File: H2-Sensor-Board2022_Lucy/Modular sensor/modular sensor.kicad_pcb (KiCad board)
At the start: 2 copper layers, 55.1 x 30.5 mm, 8 parts, among them J1 Conn_01x03_Pin

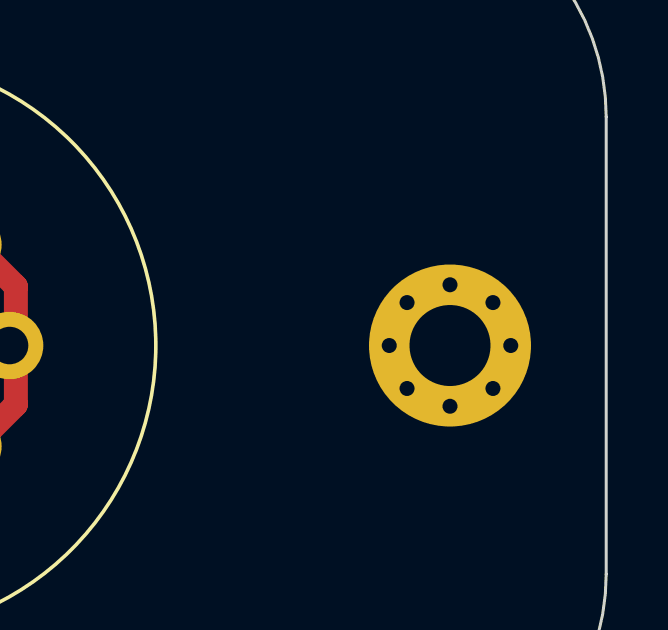
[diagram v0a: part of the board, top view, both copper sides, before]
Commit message: Started Layout fixed footprint for daughter baord and added M3 mounting holes.
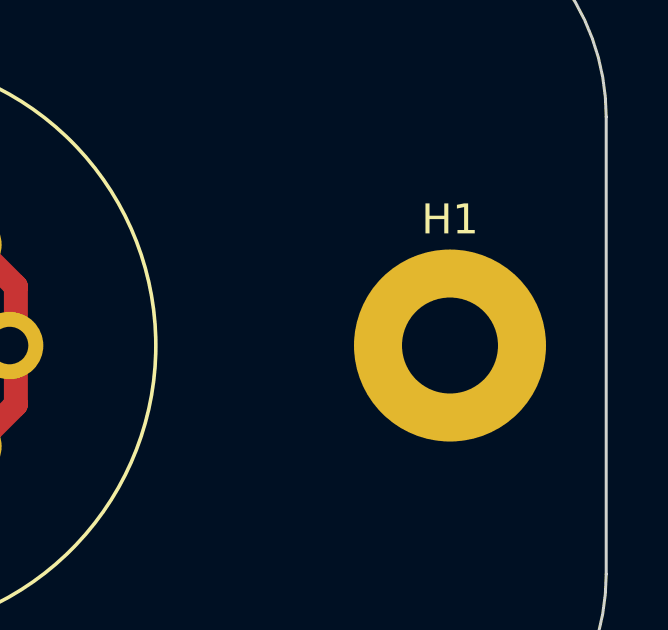
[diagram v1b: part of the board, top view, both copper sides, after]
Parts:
- H1: footprint MountingHole:MountingHole_2.7mm_M2.5_Pad_Via -> MountingHole:MountingHole_3.2mm_M3_Pad
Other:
- board text added: "Simon W."
- board text removed: "sw"
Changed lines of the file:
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@@
     )
   )
-  (footprint "MountingHole:MountingHole_2.7mm_M2.5_Pad_Via" (layer "F.Cu")
+  (footprint "MountingHole:MountingHole_3.2mm_M3_Pad" (layer "F.Cu")
     (at 169.291 93.98)
-    (descr "Mounting Hole 2.7mm")
-    (tags "mounting hole 2.7mm")
+    (descr "Mounting Hole 3.2mm, M3")
+    (tags "mounting hole 3.2mm m3")
     (property "Sheetfile" "modular sensor.kicad_sch")
     (property "Sheetname" "")
@@
     (property "ki_keywords" "mounting hole")
     (attr exclude_from_pos_files)
-    (fp_text reference "H1" (at 0 -3.7) (layer "F.SilkS") hide
+    (fp_text reference "H1" (at 0 -4.2) (layer "F.SilkS")
         (effects (font (size 1 1) (thickness 0.15)))
     )
-    (fp_text value "MountingHole_Pad" (at -2.293 4.323309) (layer "F.Fab")
+    (fp_text value "MountingHole_Pad" (at 0 4.2) (layer "F.Fab")
         (effects (font (size 1 1) (thickness 0.15)))
     )
@@
         (effects (font (size 1 1) (thickness 0.15)))
     )
-    (fp_circle (center 0 0) (end 2.7 0)
+    (fp_circle (center 0 0) (end 3.2 0)
       (stroke (width 0.15) (type solid)) (fill none) (layer "Cmts.User"))
-    (fp_circle (center 0 0) (end 2.95 0)
+    (fp_circle (center 0 0) (end 3.45 0)
       (stroke (width 0.05) (type solid)) (fill none) (layer "F.CrtYd"))
-    (pad "1" thru_hole circle (at -2.025 0) (size 0.8 0.8) (drill 0.5) (layers "*.Cu" "*.Mask")
-      (net 4 "unconnected-(H1-Pad1)") (pinfunction "1") (pintype "input"))
-    (pad "1" thru_hole circle (at -1.431891 -1.431891) (size 0.8 0.8) (drill 0.5) (layers "*.Cu" "*.Mask")
-      (net 4 "unconnected-(H1-Pad1)") (pinfunction "1") (pintype "input"))
-    (pad "1" thru_hole circle (at -1.431891 1.431891) (size 0.8 0.8) (drill 0.5) (layers "*.Cu" "*.Mask")
-      (net 4 "unconnected-(H1-Pad1)") (pinfunction "1") (pintype "input"))
-    (pad "1" thru_hole circle (at 0 -2.025) (size 0.8 0.8) (drill 0.5) (layers "*.Cu" "*.Mask")
-      (net 4 "unconnected-(H1-Pad1)") (pinfunction "1") (pintype "input"))
-    (pad "1" thru_hole circle (at 0 0) (size 5.4 5.4) (drill 2.7) (property pad_prop_castellated) (layers "*.Cu" "*.Mask")
-      (net 4 "unconnected-(H1-Pad1)") (pinfunction "1") (pintype "input"))
-    (pad "1" thru_hole circle (at 0 2.025) (size 0.8 0.8) (drill 0.5) (layers "*.Cu" "*.Mask")
-      (net 4 "unconnected-(H1-Pad1)") (pinfunction "1") (pintype "input"))
-    (pad "1" thru_hole circle (at 1.431891 -1.431891) (size 0.8 0.8) (drill 0.5) (layers "*.Cu" "*.Mask")
-      (net 4 "unconnected-(H1-Pad1)") (pinfunction "1") (pintype "input"))
-    (pad "1" thru_hole circle (at 1.431891 1.431891) (size 0.8 0.8) (drill 0.5) (layers "*.Cu" "*.Mask")
-      (net 4 "unconnected-(H1-Pad1)") (pinfunction "1") (pintype "input"))
-    (pad "1" thru_hole circle (at 2.025 0) (size 0.8 0.8) (drill 0.5) (layers "*.Cu" "*.Mask")
+    (pad "1" thru_hole circle (at 0 0) (size 6.4 6.4) (drill 3.2) (layers "*.Cu" "*.Mask")
       (net 4 "unconnected-(H1-Pad1)") (pinfunction "1") (pintype "input"))
   )
@@
     (effects (font (size 1 1) (thickness 0.2) bold) (justify left bottom mirror))
   )
-  (gr_text "sw" (at 167.64 106.68) (layer "B.SilkS")
-    (effects (font (size 1 1) (thickness 0.15)) (justify left bottom mirror))
+  (gr_text "Simon W." (at 143.383 88.392) (layer "B.SilkS")
+    (effects (font (size 1 1) (thickness 0.2) bold) (justify left bottom mirror))
   )
   (gr_text "5V" (at 124.46 96.52) (layer "F.SilkS")

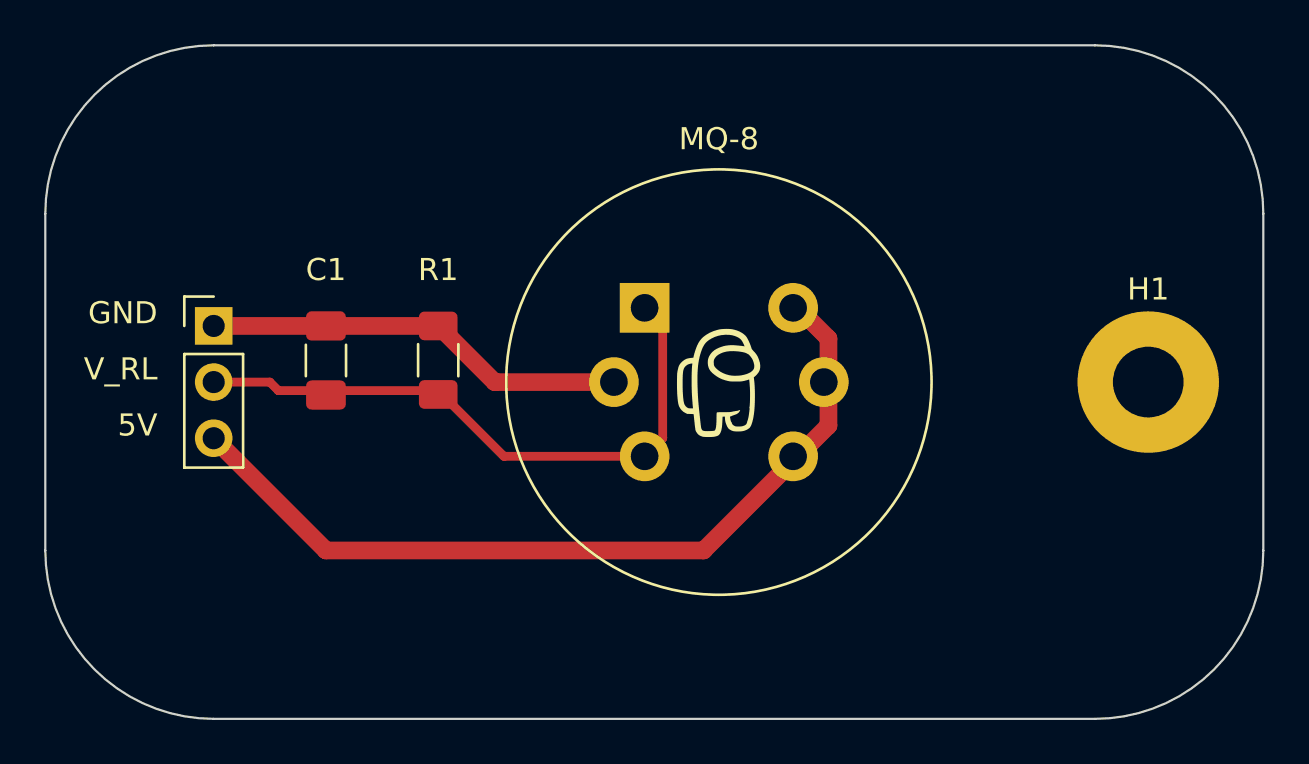
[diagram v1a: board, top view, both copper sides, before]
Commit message: Added all required components made modular sensor smaller and and laid out main board
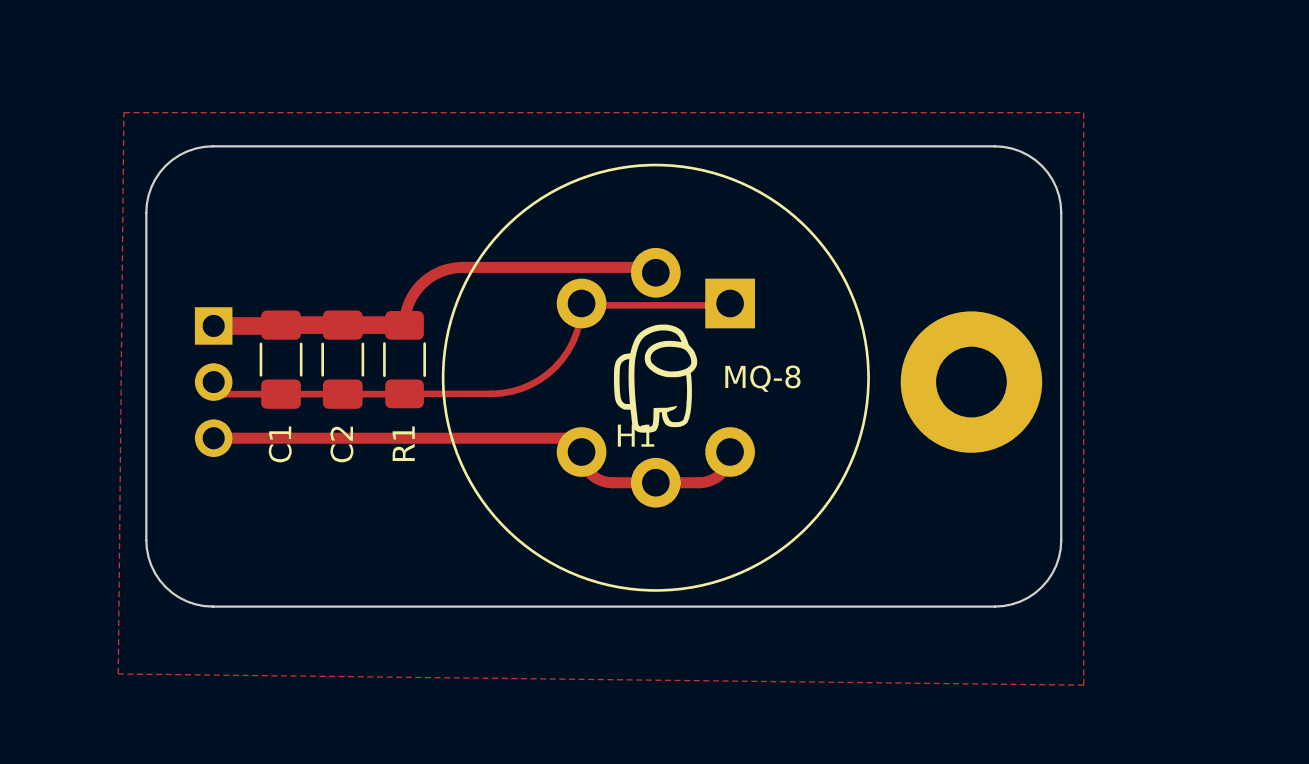
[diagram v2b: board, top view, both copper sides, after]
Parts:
- added C2: 100uF, Capacitor_SMD:C_1206_3216Metric_Pad1.33x1.80mm_HandSolder, F.Cu at (132.8, 93.0)
- J1: moved to B.Cu
- R1: value 4.7k Ω -> 4k7
- moved H1 8.00 mm to (161.3, 94.0)
- moved G*** 5.78 mm to (152.6, 86.8)
- moved G*** 5.73 mm to (155.1, 86.8)
- moved MQ-8 3.87 mm to (150.4, 90.4), turned to -90 degrees
- moved G*** 2.86 mm to (147.0, 93.8)
- moved C1 2.03 mm to (130.0, 93.0)
- moved R1 1.52 mm to (135.6, 93.0)
- turned J1 to 180 degrees
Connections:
- net V_RL renamed /V_RL
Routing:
- net +5V: track 38.2 -> 25.1 mm
- net /V_RL: track 28.3 -> 25.8 mm
- net GND: track 19.2 -> 21.5 mm
- added copper zone on F.Cu, net GND
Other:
- board size 55.1 x 30.5 mm -> 41.4 x 20.8 mm

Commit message: I am highly sleep deprived
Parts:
- removed C1: 50nF, Capacitor_SMD:C_1206_3216Metric_Pad1.33x1.80mm_HandSolder
- removed C2: 100uF, Capacitor_SMD:C_1206_3216Metric_Pad1.33x1.80mm_HandSolder
- removed R1: 4k7, Resistor_SMD:R_1206_3216Metric_Pad1.30x1.75mm_HandSolder
- moved G*** 8.61 mm to (144.0, 86.6)
- moved G*** 8.61 mm to (146.5, 86.6)
- moved H1 8.38 mm to (152.9, 94.0)
- moved G*** 7.38 mm to (139.6, 94.3)
- moved MQ-8 7.38 mm to (143.0, 90.9)
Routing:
- net GND: track 21.5 -> 13.4 mm
- net /V_RL: track 25.8 -> 18.3 mm
- net +5V: track 25.1 -> 17.9 mm
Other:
- board size 41.4 x 20.8 mm -> 31.8 x 20.3 mm
- board text removed: "GND"
